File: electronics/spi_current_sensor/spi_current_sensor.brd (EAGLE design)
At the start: 44.5 x 24.1 mm, 3 parts, among them J2 METALTEX-2, U1 TLI4970_D025T5

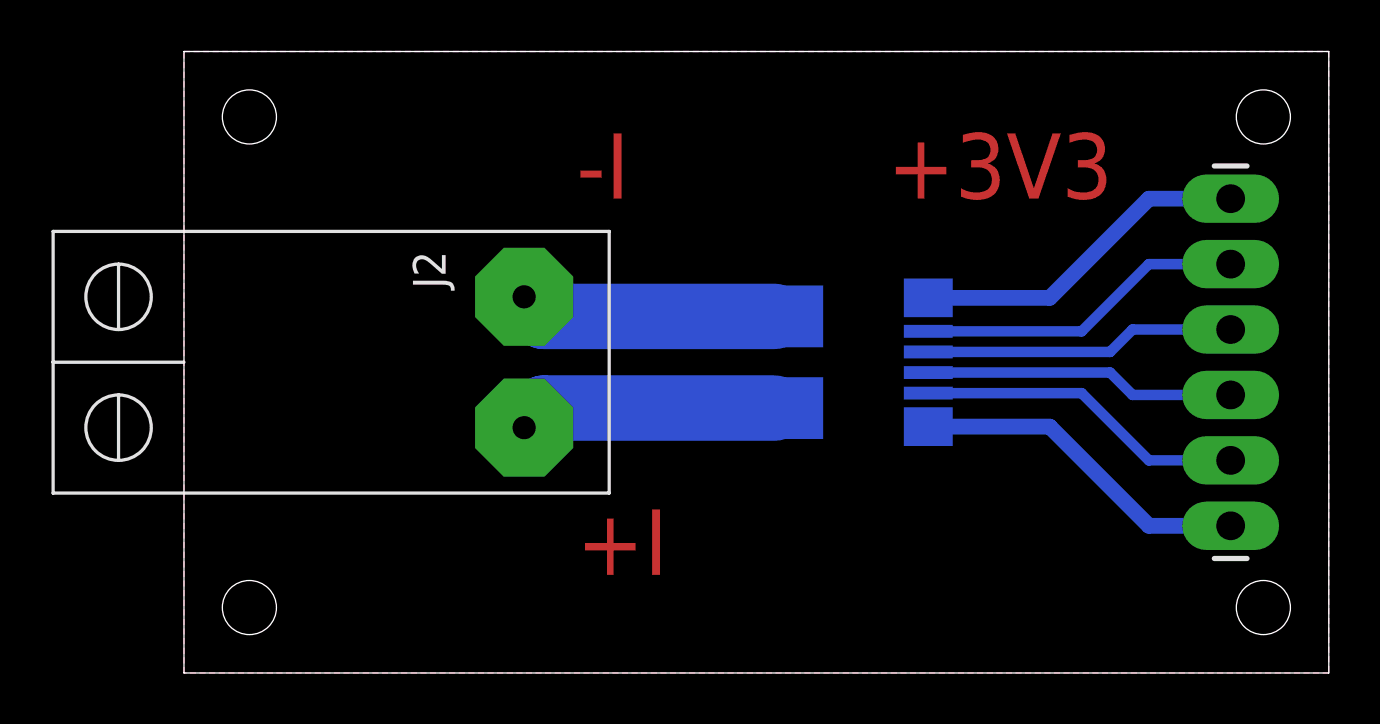
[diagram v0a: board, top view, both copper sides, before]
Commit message: Add decoupler capacitor to current sensor
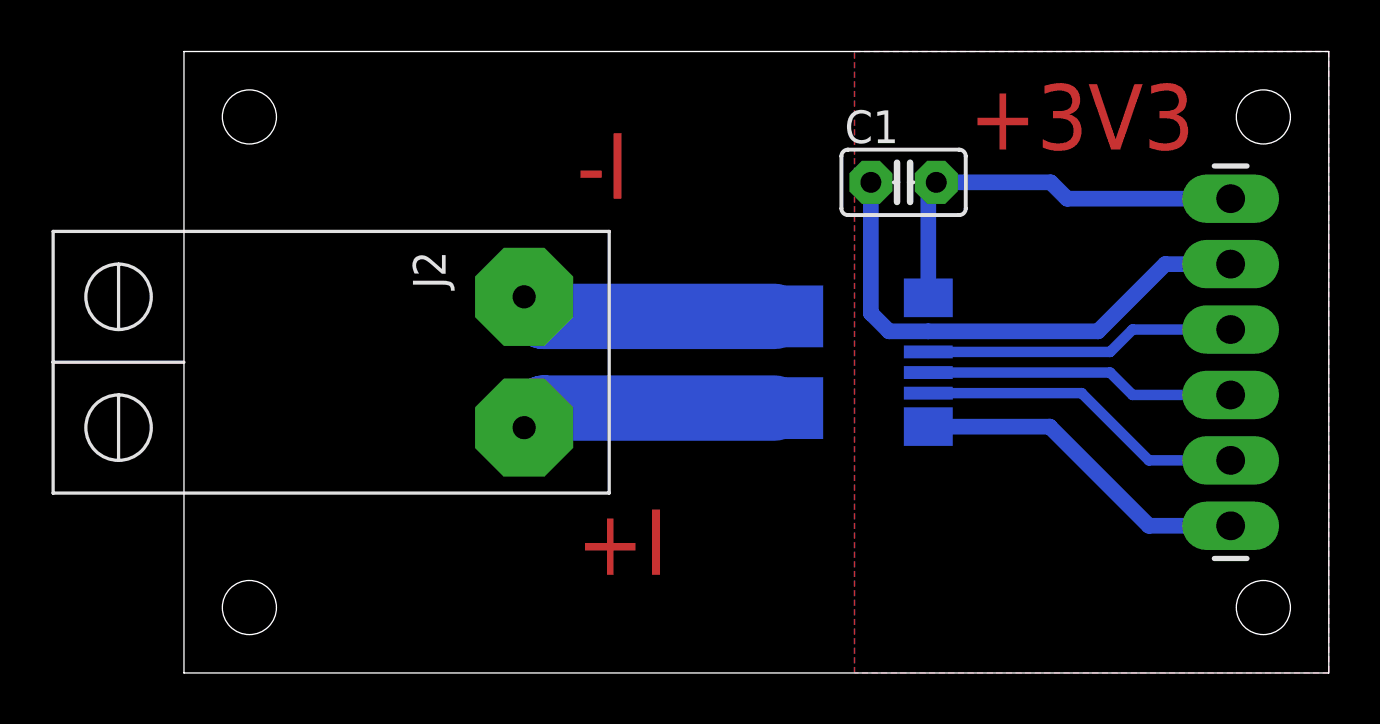
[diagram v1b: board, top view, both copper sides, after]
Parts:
- added C1: 0.1u, adafruit:C025-025X050
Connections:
- net +3V3: now also C1.1, J1.2, U1.2; no longer J1.1, U1.1
- net GND: now also C1.2, J1.1, U1.1; no longer J1.2, U1.2
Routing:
- net +3V3: track 13.3 -> 20.4 mm
- net GND: track 12.8 -> 16.3 mm
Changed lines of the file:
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@@
 <setting verticaltext="up"/>
 </settings>
-<grid distance="1" unitdist="mm" unit="mm" style="lines" multiple="1" display="yes" altdistance="0.025" altunitdist="inch" altunit="inch"/>
+<grid distance="100" unitdist="mil" unit="mil" style="lines" multiple="1" display="yes" altdistance="0.025" altunitdist="inch" altunit="inch"/>
 <layers>
 <layer number="1" name="Top" color="4" fill="1" visible="yes" active="yes"/>
@@
 <text x="15.24" y="18.415" size="2.54" layer="1" font="vector" ratio="20">-I</text>
 <text x="15.24" y="3.81" size="2.54" layer="1" font="vector" ratio="20">+I</text>
-<text x="27.305" y="18.415" size="2.54" layer="1" font="vector" ratio="20">+3V3</text>
+<text x="30.48" y="20.32" size="2.54" layer="1" font="vector" ratio="20">+3V3</text>
 <hole x="2.54" y="21.59" drill="2.1"/>
 <hole x="2.54" y="2.54" drill="2.1"/>
@@
 <element name="J2" library="uchile_robotics_eagle_lib" package="METALTEX-2" value="METALTEX-2" x="11.43" y="12.065" rot="R270"/>
 <element name="U1" library="uchile_robotics_eagle_lib" package="TLI4970_D025T5" value="TLI4970_D025T5" x="25.4" y="12.065" smashed="yes" rot="MR270">
-<attribute name="VALUE" x="19.725" y="17.065" size="1.016" layer="28" font="vector" rot="MR180"/>
 <attribute name="NAME" x="24.17" y="8.065" size="1.016" layer="26" font="vector" rot="MR180"/>
+</element>
+<element name="C1" library="adafruit" package="C025-025X050" value="0.1u" x="27.94" y="19.05" smashed="yes">
+<attribute name="NAME" x="25.654" y="20.574" size="1.27" layer="25" ratio="10"/>
 </element>
 </elements>
 <signals>
-<signal name="+3V3">
+<signal name="GND">
+<contactref element="U1" pad="1"/>
+<contactref element="C1" pad="2"/>
 <contactref element="J1" pad="1"/>
-<contactref element="U1" pad="1"/>
-<wire x1="28.9" y1="14.565" x2="33.615" y2="14.565" width="0.6096" layer="16"/>
-<wire x1="33.615" y1="14.565" x2="37.465" y2="18.415" width="0.6096" layer="16"/>
-<wire x1="37.465" y1="18.415" x2="40.64" y2="18.415" width="0.6096" layer="16"/>
-</signal>
-<signal name="GND">
-<contactref element="J1" pad="2"/>
-<contactref element="U1" pad="2"/>
-<wire x1="28.9" y1="13.265" x2="34.855" y2="13.265" width="0.4064" layer="16"/>
-<wire x1="34.855" y1="13.265" x2="37.465" y2="15.875" width="0.4064" layer="16"/>
-<wire x1="37.465" y1="15.875" x2="40.64" y2="15.875" width="0.4064" layer="16"/>
+<wire x1="28.9" y1="14.565" x2="28.9" y2="18.74" width="0.6096" layer="16"/>
+<wire x1="28.9" y1="18.74" x2="29.21" y2="19.05" width="0.4064" layer="16"/>
+<wire x1="29.21" y1="19.05" x2="33.655" y2="19.05" width="0.6096" layer="16"/>
+<wire x1="33.655" y1="19.05" x2="34.29" y2="18.415" width="0.6096" layer="16"/>
+<wire x1="34.29" y1="18.415" x2="40.64" y2="18.415" width="0.6096" layer="16"/>
 </signal>
 <signal name="N$1">
@@
 <signal name="N$7">
 <polygon width="0.4064" layer="16" isolate="1.016">
-<vertex x="0" y="24.13"/>
+<vertex x="26.035" y="24.13"/>
 <vertex x="44.45" y="24.13"/>
 <vertex x="44.45" y="0"/>
-<vertex x="0" y="0"/>
+<vertex x="26.035" y="0"/>
 </polygon>
 </signal>
 <signal name="N$8">
 <polygon width="0.4064" layer="1" isolate="1.016">
-<vertex x="0" y="24.13"/>
+<vertex x="26.035" y="24.13"/>
 <vertex x="44.45" y="24.13"/>
 <vertex x="44.45" y="0"/>
-<vertex x="0" y="0"/>
+<vertex x="26.035" y="0"/>
 </polygon>
 </signal>
+<signal name="+3V3">
+<contactref element="U1" pad="2"/>
+<contactref element="C1" pad="1"/>
+<contactref element="J1" pad="2"/>
+<wire x1="28.9" y1="13.265" x2="35.49" y2="13.265" width="0.6096" layer="16"/>
+<wire x1="35.49" y1="13.265" x2="38.1" y2="15.875" width="0.6096" layer="16"/>
+<wire x1="38.1" y1="15.875" x2="40.64" y2="15.875" width="0.6096" layer="16"/>
+<wire x1="28.9" y1="13.265" x2="27.375" y2="13.265" width="0.6096" layer="16"/>
+<wire x1="27.375" y1="13.265" x2="26.67" y2="13.97" width="0.6096" layer="16"/>
+<wire x1="26.67" y1="13.97" x2="26.67" y2="19.05" width="0.6096" layer="16"/>
+</signal>
 </signals>
